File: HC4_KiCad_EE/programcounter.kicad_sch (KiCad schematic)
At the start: 14 parts, among them IC10 74HC161, IC9 74HC161

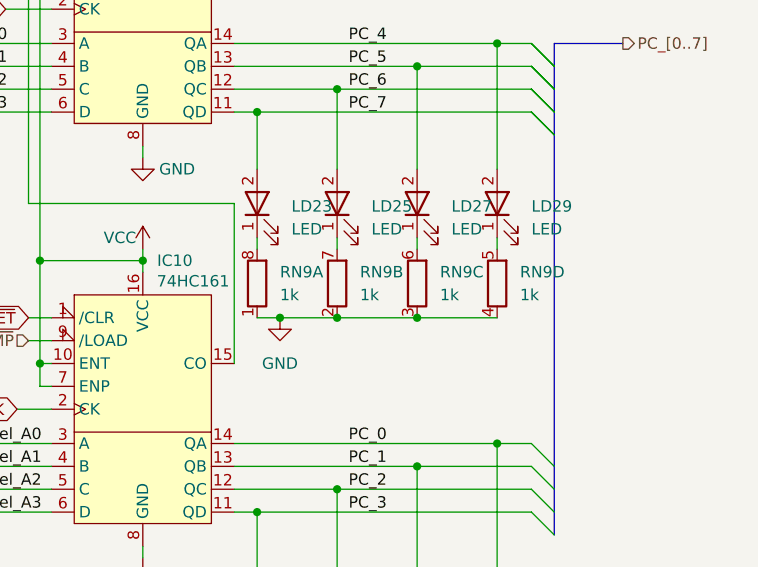
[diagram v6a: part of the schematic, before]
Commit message: 配線進捗、7474を使った変な回路
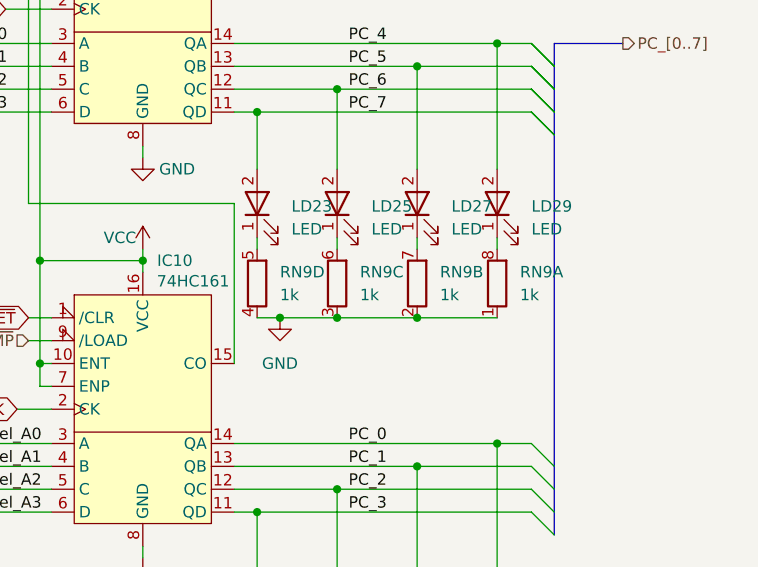
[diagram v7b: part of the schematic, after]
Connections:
- net at LD29.1 (K): now also RN9.8 (R1.2); no longer RN9.5 (R4.2)
- net at LD25.1 (K): now also RN9.6 (R3.2); no longer RN9.7 (R2.2)
- net at LD27.1 (K): now also RN9.7 (R2.2); no longer RN9.6 (R3.2)
- net at LD23.1 (K): now also RN9.5 (R4.2); no longer RN9.8 (R1.2)
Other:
- moved on the sheet: RN9A, RN9B, RN9C, RN9D
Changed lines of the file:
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@@
+	)
+	(junction
+		(at 148.59 125.73)
+		(diameter 0)
+		(color 0 0 0 0)
 	)
 	(junction
@@
 	)
 	(junction
-		(at 148.59 125.73)
-		(diameter 0)
-		(color 0 0 0 0)
-	)
-	(junction
 		(at 166.37 95.25)
 		(diameter 0)
@@
 	(wire
 		(pts
+			(xy 148.59 125.73) (xy 157.48 125.73)
+		)
+		(stroke
+			(width 0)
+			(type default)
+		)
+	)
+	(wire
+		(pts
 			(xy 118.11 175.26) (xy 118.11 173.99)
 		)
@@
 	(wire
 		(pts
+			(xy 139.7 125.73) (xy 142.24 125.73)
+		)
+		(stroke
+			(width 0)
+			(type default)
+		)
+	)
+	(wire
+		(pts
 			(xy 114.3 81.28) (xy 116.84 81.28)
 		)
@@
 	(wire
 		(pts
+			(xy 157.48 125.73) (xy 166.37 125.73)
+		)
+		(stroke
+			(width 0)
+			(type default)
+		)
+	)
+	(wire
+		(pts
 			(xy 139.7 102.87) (xy 137.16 102.87)
 		)
@@
 	(wire
 		(pts
-			(xy 139.7 125.73) (xy 142.24 125.73)
-		)
-		(stroke
-			(width 0)
-			(type default)
-		)
-	)
-	(wire
-		(pts
 			(xy 107.95 139.7) (xy 116.84 139.7)
 		)
@@
 	(wire
 		(pts
-			(xy 148.59 125.73) (xy 157.48 125.73)
-		)
-		(stroke
-			(width 0)
-			(type default)
-		)
-	)
-	(wire
-		(pts
 			(xy 166.37 139.7) (xy 170.18 139.7)
 		)
@@
 		(pts
 			(xy 124.46 184.15) (xy 137.16 184.15)
-		)
-		(stroke
-			(width 0)
-			(type default)
-		)
-	)
-	(wire
-		(pts
-			(xy 157.48 125.73) (xy 166.37 125.73)
 		)
 		(stroke
@@
 	(symbol
 		(lib_id "Device:R_Pack04_Split")
-		(at 148.59 121.92 0)
+		(at 157.48 121.92 0)
 		(unit 2)
 		(exclude_from_sim no)
@@
 		(on_board yes)
 		(dnp no)
-		(fields_autoplaced yes)
 		(property "Reference" "RN9"
-			(at 151.13 120.6499 0)
+			(at 160.02 120.6499 0)
 			(effects
 				(font
@@
 		)
 		(property "Value" "1k"
-			(at 151.13 123.1899 0)
+			(at 160.02 123.1899 0)
 			(effects
 				(font
@@
 		)
 		(property "Footprint" "Resistor_SMD:R_Array_Convex_4x0603"
-			(at 146.558 121.92 90)
+			(at 155.448 121.92 90)
 			(effects
 				(font
@@
 		)
 		(property "Datasheet" "~"
-			(at 148.59 121.92 0)
+			(at 157.48 121.92 0)
 			(effects
 				(font
@@
 		)
 		(property "Description" "4 resistor network, parallel topology, split"
-			(at 148.59 121.92 0)
+			(at 157.48 121.92 0)
 			(effects
 				(font
@@
 	(symbol
 		(lib_id "Device:R_Pack04_Split")
-		(at 166.37 121.92 0)
+		(at 139.7 121.92 0)
 		(unit 4)
 		(exclude_from_sim no)
@@
 		(on_board yes)
 		(dnp no)
-		(fields_autoplaced yes)
 		(property "Reference" "RN9"
-			(at 168.91 120.6499 0)
+			(at 142.24 120.6499 0)
 			(effects
 				(font
@@
 		)
 		(property "Value" "1k"
-			(at 168.91 123.1899 0)
+			(at 142.24 123.1899 0)
 			(effects
 				(font
@@
 		)
 		(property "Footprint" "Resistor_SMD:R_Array_Convex_4x0603"
-			(at 164.338 121.92 90)
+			(at 137.668 121.92 90)
 			(effects
 				(font
@@
 		)
 		(property "Datasheet" "~"
-			(at 166.37 121.92 0)
+			(at 139.7 121.92 0)
 			(effects
 				(font
@@
 		)
 		(property "Description" "4 resistor network, parallel topology, split"
-			(at 166.37 121.92 0)
+			(at 139.7 121.92 0)
 			(effects
 				(font
@@
 	(symbol
 		(lib_id "Device:R_Pack04_Split")
-		(at 157.48 121.92 0)
+		(at 148.59 121.92 0)
 		(unit 3)
 		(exclude_from_sim no)
@@
 		(on_board yes)
 		(dnp no)
-		(fields_autoplaced yes)
 		(property "Reference" "RN9"
-			(at 160.02 120.6499 0)
+			(at 151.13 120.6499 0)
 			(effects
 				(font
@@
 		)
 		(property "Value" "1k"
-			(at 160.02 123.1899 0)
+			(at 151.13 123.1899 0)
 			(effects
 				(font
@@
 		)
 		(property "Footprint" "Resistor_SMD:R_Array_Convex_4x0603"
-			(at 155.448 121.92 90)
+			(at 146.558 121.92 90)
 			(effects
 				(font
@@
 		)
 		(property "Datasheet" "~"
-			(at 157.48 121.92 0)
+			(at 148.59 121.92 0)
 			(effects
 				(font
@@
 		)
 		(property "Description" "4 resistor network, parallel topology, split"
-			(at 157.48 121.92 0)
+			(at 148.59 121.92 0)
 			(effects
 				(font
@@
 	(symbol
 		(lib_id "Device:R_Pack04_Split")
-		(at 139.7 121.92 0)
+		(at 166.37 121.92 0)
 		(unit 1)
 		(exclude_from_sim no)
@@
 		(on_board yes)
 		(dnp no)
-		(fields_autoplaced yes)
 		(property "Reference" "RN9"
-			(at 142.24 120.6499 0)
+			(at 168.91 120.6499 0)
 			(effects
 				(font
@@
 		)
 		(property "Value" "1k"
-			(at 142.24 123.1899 0)
+			(at 168.91 123.1899 0)
 			(effects
 				(font
@@
 		)
 		(property "Footprint" "Resistor_SMD:R_Array_Convex_4x0603"
-			(at 137.668 121.92 90)
+			(at 164.338 121.92 90)
 			(effects
 				(font
@@
 		)
 		(property "Datasheet" "~"
-			(at 139.7 121.92 0)
+			(at 166.37 121.92 0)
 			(effects
 				(font
@@
 		)
 		(property "Description" "4 resistor network, parallel topology, split"
-			(at 139.7 121.92 0)
-			(effects
-				(font
+			(at 166.37 121.92 0)
+			(effects
+				(font

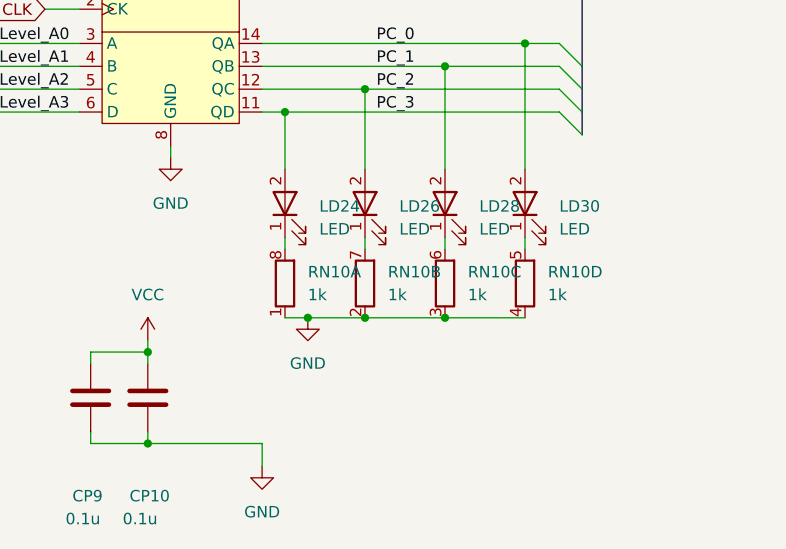
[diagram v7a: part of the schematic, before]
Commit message: LEDの抵抗を入れ替え
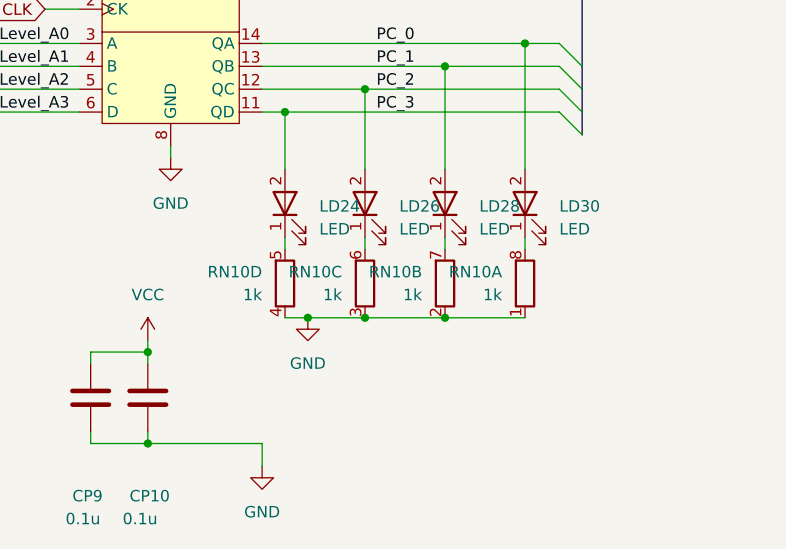
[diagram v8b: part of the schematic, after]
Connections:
- net at RN10.7 (R2.2): now also LD28.1 (K); no longer LD26.1 (K)
- net at RN10.5 (R4.2): now also LD24.1 (K); no longer LD30.1 (K)
- net at RN10.8 (R1.2): now also LD30.1 (K); no longer LD24.1 (K)
- net at RN10.6 (R3.2): now also LD26.1 (K); no longer LD28.1 (K)
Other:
- moved on the sheet: RN10A, RN10B, RN10C, RN10D
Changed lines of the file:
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@@
 	)
 	(junction
+		(at 157.48 170.18)
+		(diameter 0)
+		(color 0 0 0 0)
+	)
+	(junction
 		(at 139.7 147.32)
 		(diameter 0)
@@
 	)
 	(junction
-		(at 148.59 170.18)
-		(diameter 0)
-		(color 0 0 0 0)
-	)
-	(junction
 		(at 124.46 184.15)
 		(diameter 0)
@@
 	)
 	(junction
-		(at 157.48 170.18)
+		(at 148.59 170.18)
 		(diameter 0)
 		(color 0 0 0 0)
@@
 	(wire
 		(pts
+			(xy 148.59 170.18) (xy 157.48 170.18)
+		)
+		(stroke
+			(width 0)
+			(type default)
+		)
+	)
+	(wire
+		(pts
 			(xy 127 118.11) (xy 127 119.38)
 		)
@@
 	(wire
 		(pts
-			(xy 139.7 147.32) (xy 139.7 153.67)
+			(xy 157.48 170.18) (xy 166.37 170.18)
 		)
 		(stroke
@@
 	(wire
 		(pts
-			(xy 148.59 170.18) (xy 157.48 170.18)
+			(xy 139.7 147.32) (xy 139.7 153.67)
 		)
 		(stroke
@@
 		)
 	)
-	(wire
-		(pts
-			(xy 142.24 170.18) (xy 148.59 170.18)
-		)
-		(stroke
-			(width 0)
-			(type default)
-		)
-	)
 	(bus
 		(pts
@@
 	(wire
 		(pts
-			(xy 124.46 172.72) (xy 124.46 173.99)
+			(xy 142.24 170.18) (xy 148.59 170.18)
 		)
 		(stroke
@@
 		)
 	)
-	(bus
+	(wire
 		(pts
-			(xy 172.72 102.87) (xy 172.72 105.41)
+			(xy 124.46 172.72) (xy 124.46 173.99)
 		)
 		(stroke
@@
 		)
 	)
-	(wire
+	(bus
 		(pts
-			(xy 157.48 170.18) (xy 166.37 170.18)
+			(xy 172.72 102.87) (xy 172.72 105.41)
 		)
 		(stroke
@@
 	(symbol
 		(lib_id "Device:R_Pack04_Split")
-		(at 148.59 166.37 0)
+		(at 157.48 166.37 0)
+		(mirror y)
 		(unit 2)
 		(exclude_from_sim no)
@@
 		(fields_autoplaced yes)
 		(property "Reference" "RN10"
-			(at 151.13 165.0999 0)
+			(at 154.94 165.0999 0)
 			(effects
 				(font
@@
 		)
 		(property "Value" "1k"
-			(at 151.13 167.6399 0)
+			(at 154.94 167.6399 0)
 			(effects
 				(font
@@
 		)
 		(property "Footprint" "Resistor_SMD:R_Array_Convex_4x0603"
-			(at 146.558 166.37 90)
+			(at 159.512 166.37 90)
 			(effects
 				(font
@@
 		)
 		(property "Datasheet" "~"
-			(at 148.59 166.37 0)
+			(at 157.48 166.37 0)
 			(effects
 				(font
@@
 		)
 		(property "Description" "4 resistor network, parallel topology, split"
-			(at 148.59 166.37 0)
+			(at 157.48 166.37 0)
 			(effects
 				(font
@@
 	(symbol
 		(lib_id "Device:R_Pack04_Split")
-		(at 166.37 166.37 0)
+		(at 139.7 166.37 0)
+		(mirror y)
 		(unit 4)
 		(exclude_from_sim no)
@@
 		(fields_autoplaced yes)
 		(property "Reference" "RN10"
-			(at 168.91 165.0999 0)
+			(at 137.16 165.0999 0)
 			(effects
 				(font
@@
 		)
 		(property "Value" "1k"
-			(at 168.91 167.6399 0)
+			(at 137.16 167.6399 0)
 			(effects
 				(font
@@
 		)
 		(property "Footprint" "Resistor_SMD:R_Array_Convex_4x0603"
-			(at 164.338 166.37 90)
+			(at 141.732 166.37 90)
 			(effects
 				(font
@@
 		)
 		(property "Datasheet" "~"
-			(at 166.37 166.37 0)
+			(at 139.7 166.37 0)
 			(effects
 				(font
@@
 		)
 		(property "Description" "4 resistor network, parallel topology, split"
-			(at 166.37 166.37 0)
+			(at 139.7 166.37 0)
 			(effects
 				(font
@@
 	(symbol
 		(lib_id "Device:R_Pack04_Split")
-		(at 139.7 166.37 0)
+		(at 166.37 166.37 0)
+		(mirror y)
 		(unit 1)
 		(exclude_from_sim no)
@@
 		(fields_autoplaced yes)
 		(property "Reference" "RN10"
-			(at 142.24 165.0999 0)
+			(at 163.83 165.0999 0)
 			(effects
 				(font
@@
 		)
 		(property "Value" "1k"
-			(at 142.24 167.6399 0)
+			(at 163.83 167.6399 0)
 			(effects
 				(font
@@
 		)
 		(property "Footprint" "Resistor_SMD:R_Array_Convex_4x0603"
-			(at 137.668 166.37 90)
+			(at 168.402 166.37 90)
 			(effects
 				(font
@@
 		)
 		(property "Datasheet" "~"
-			(at 139.7 166.37 0)
+			(at 166.37 166.37 0)
 			(effects
 				(font
@@
 		)
 		(property "Description" "4 resistor network, parallel topology, split"
-			(at 139.7 166.37 0)
+			(at 166.37 166.37 0)
 			(effects
 				(font
@@
 	(symbol
 		(lib_id "Device:R_Pack04_Split")
-		(at 157.48 166.37 0)
+		(at 148.59 166.37 0)
+		(mirror y)
 		(unit 3)
 		(exclude_from_sim no)
@@
 		(fields_autoplaced yes)
 		(property "Reference" "RN10"
-			(at 160.02 165.0999 0)
+			(at 146.05 165.0999 0)
 			(effects
 				(font
@@
 		)
 		(property "Value" "1k"
-			(at 160.02 167.6399 0)
+			(at 146.05 167.6399 0)
 			(effects
 				(font
@@
 		)
 		(property "Footprint" "Resistor_SMD:R_Array_Convex_4x0603"
-			(at 155.448 166.37 90)
+			(at 150.622 166.37 90)
 			(effects
 				(font
@@
 		)
 		(property "Datasheet" "~"
-			(at 157.48 166.37 0)
+			(at 148.59 166.37 0)
 			(effects
 				(font
@@
 		)
 		(property "Description" "4 resistor network, parallel topology, split"
-			(at 157.48 166.37 0)
+			(at 148.59 166.37 0)
 			(effects
 				(font
